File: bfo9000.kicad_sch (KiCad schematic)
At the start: 122 parts, among them U1 ProMicro, U2 TRRS, U3 TRRS

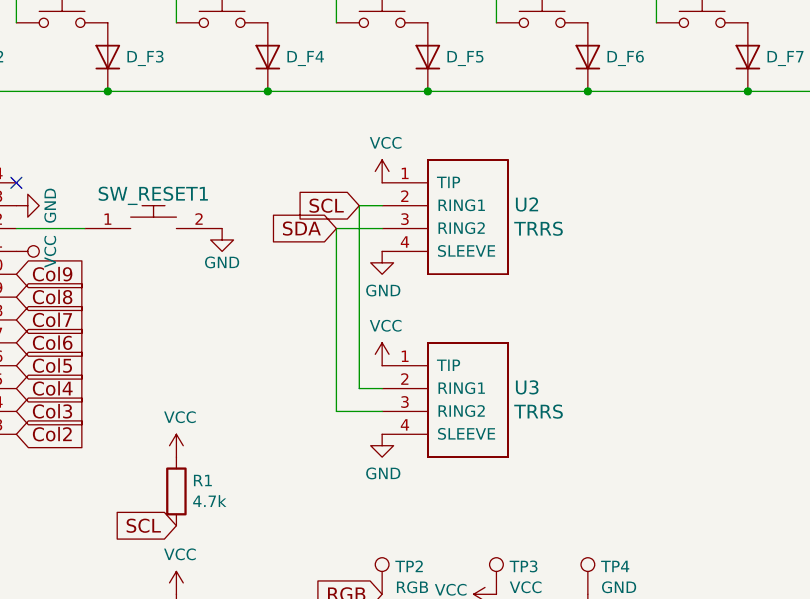
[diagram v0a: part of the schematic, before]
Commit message: Fix TRRS plug pinout
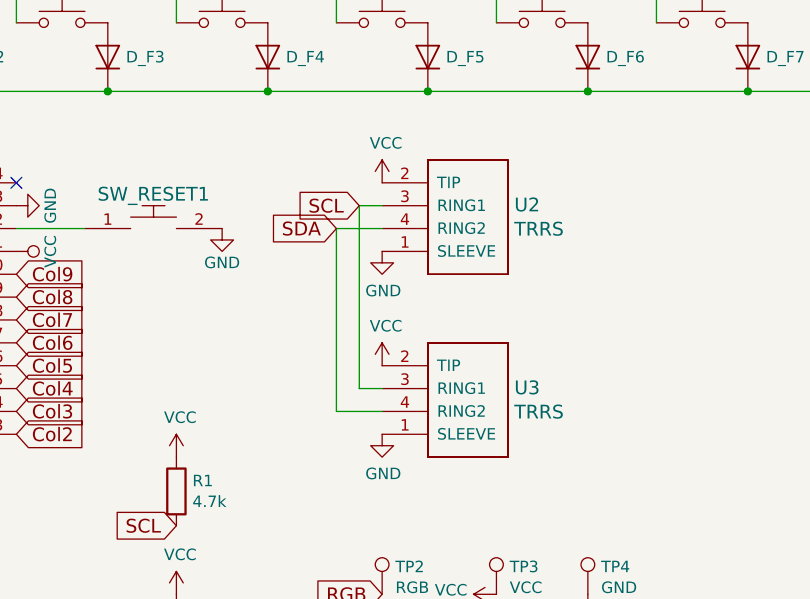
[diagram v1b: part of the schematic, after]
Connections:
- net GND: now also U2.1 (SLEEVE), U3.1 (SLEEVE); no longer U2.4 (SLEEVE), U3.4 (SLEEVE)
- net SCL: now also U2.3 (RING1), U3.3 (RING1); no longer U2.2 (RING1), U3.2 (RING1)
- net SDA: now also U2.4 (RING2), U3.4 (RING2); no longer U2.3 (RING2), U3.3 (RING2)
- net VCC: now also U2.2 (TIP), U3.2 (TIP); no longer U2.1 (TIP), U3.1 (TIP)
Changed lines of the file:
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@@
     )
   )
-  (symbol (lib_id "bfo9000-rescue:TRRS-keebio") (at 115.57 134.62 0) (unit 1)
+  (symbol (lib_name "TRRS-keebio_1") (lib_id "bfo9000-rescue:TRRS-keebio") (at 115.57 134.62 0) (unit 1)
     (in_bom yes) (on_board yes)
     (property "Reference" "U2" (id 0) (at 121.3612 126.9238 0)
@@
       (effects (font (size 1.524 1.524)) hide)
     )
-    (pin "1")
     (pin "2")
     (pin "3")
     (pin "4")
+    (pin "1")
   )
   (symbol (lib_id "bfo9000-rescue:TRRS-keebio") (at 115.57 154.94 0) (unit 1)
@@
       (effects (font (size 1.524 1.524)) hide)
     )
-    (pin "1")
     (pin "2")
     (pin "3")
     (pin "4")
+    (pin "1")
   )
   (symbol (lib_id "power:VCC") (at 106.68 124.46 0) (unit 1)
